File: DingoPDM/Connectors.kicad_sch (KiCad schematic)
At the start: 13 parts, among them J1 RedCubeTerminal, J2 RedCubeTerminal, J3 Conn_01x12, J5 USB_C_Receptacle_USB2.0

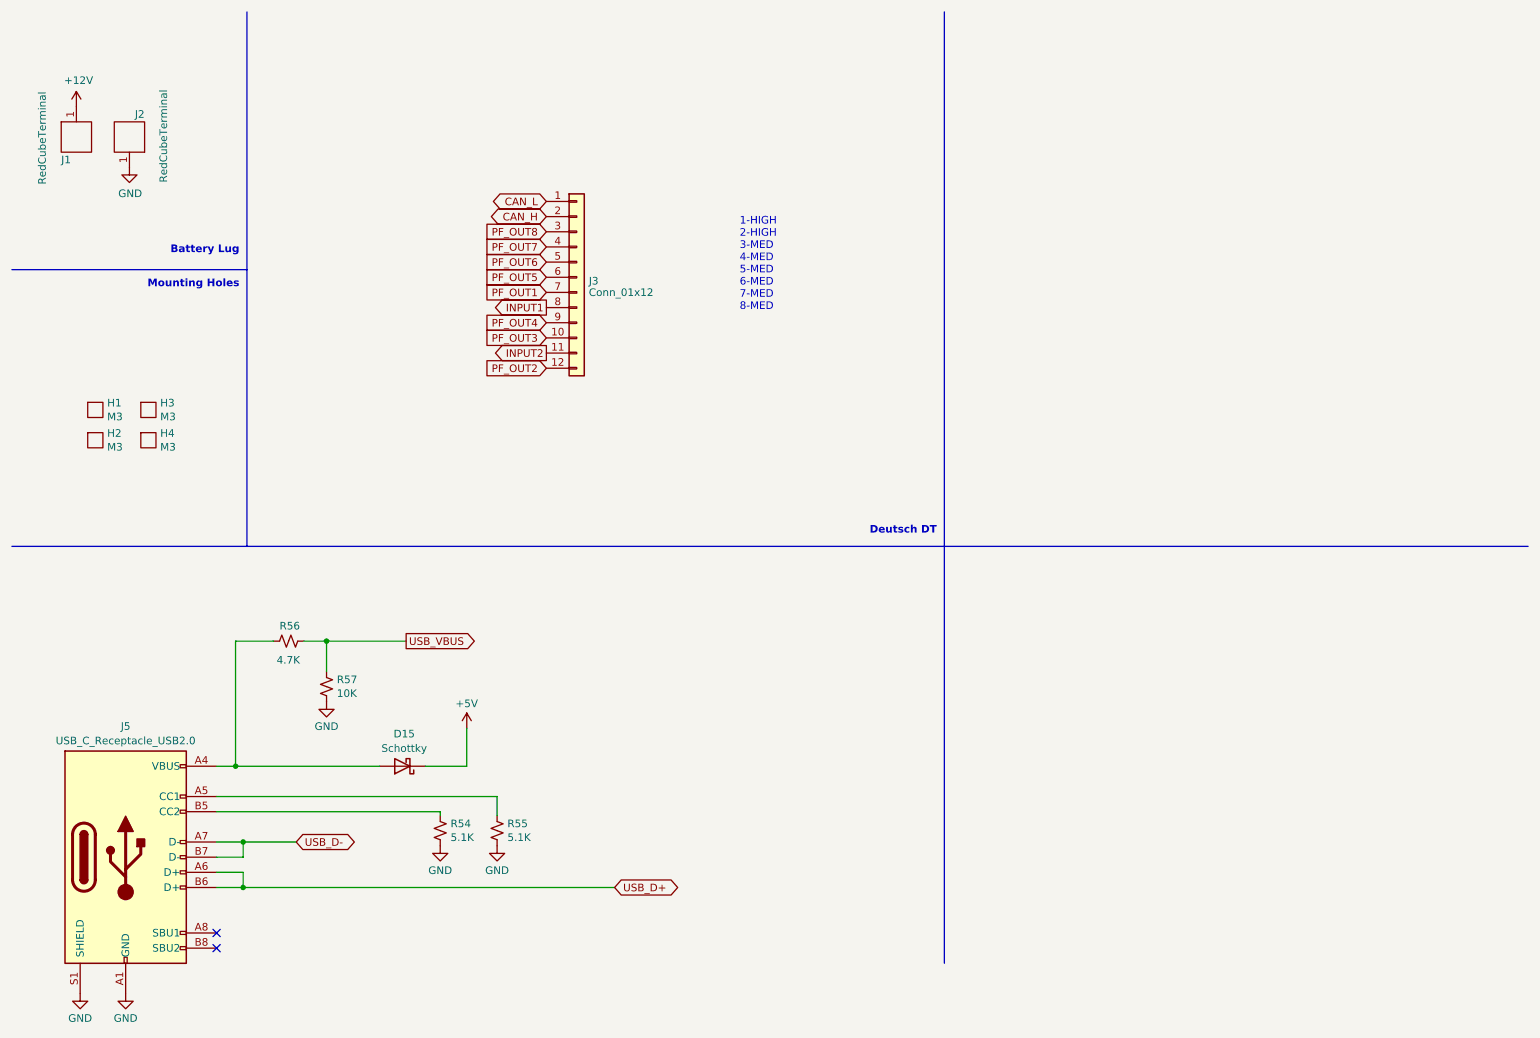
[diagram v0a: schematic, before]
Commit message: Modified PCB for 10ch PDM board
I modified the original dingoPDM for 10 channels. The board has been manufactured, tested and works but after mounting I decided that it doesn't suit my needs for the current build. I may develop it further in the future, make it pretty etc but for now I am marking this project as stale.
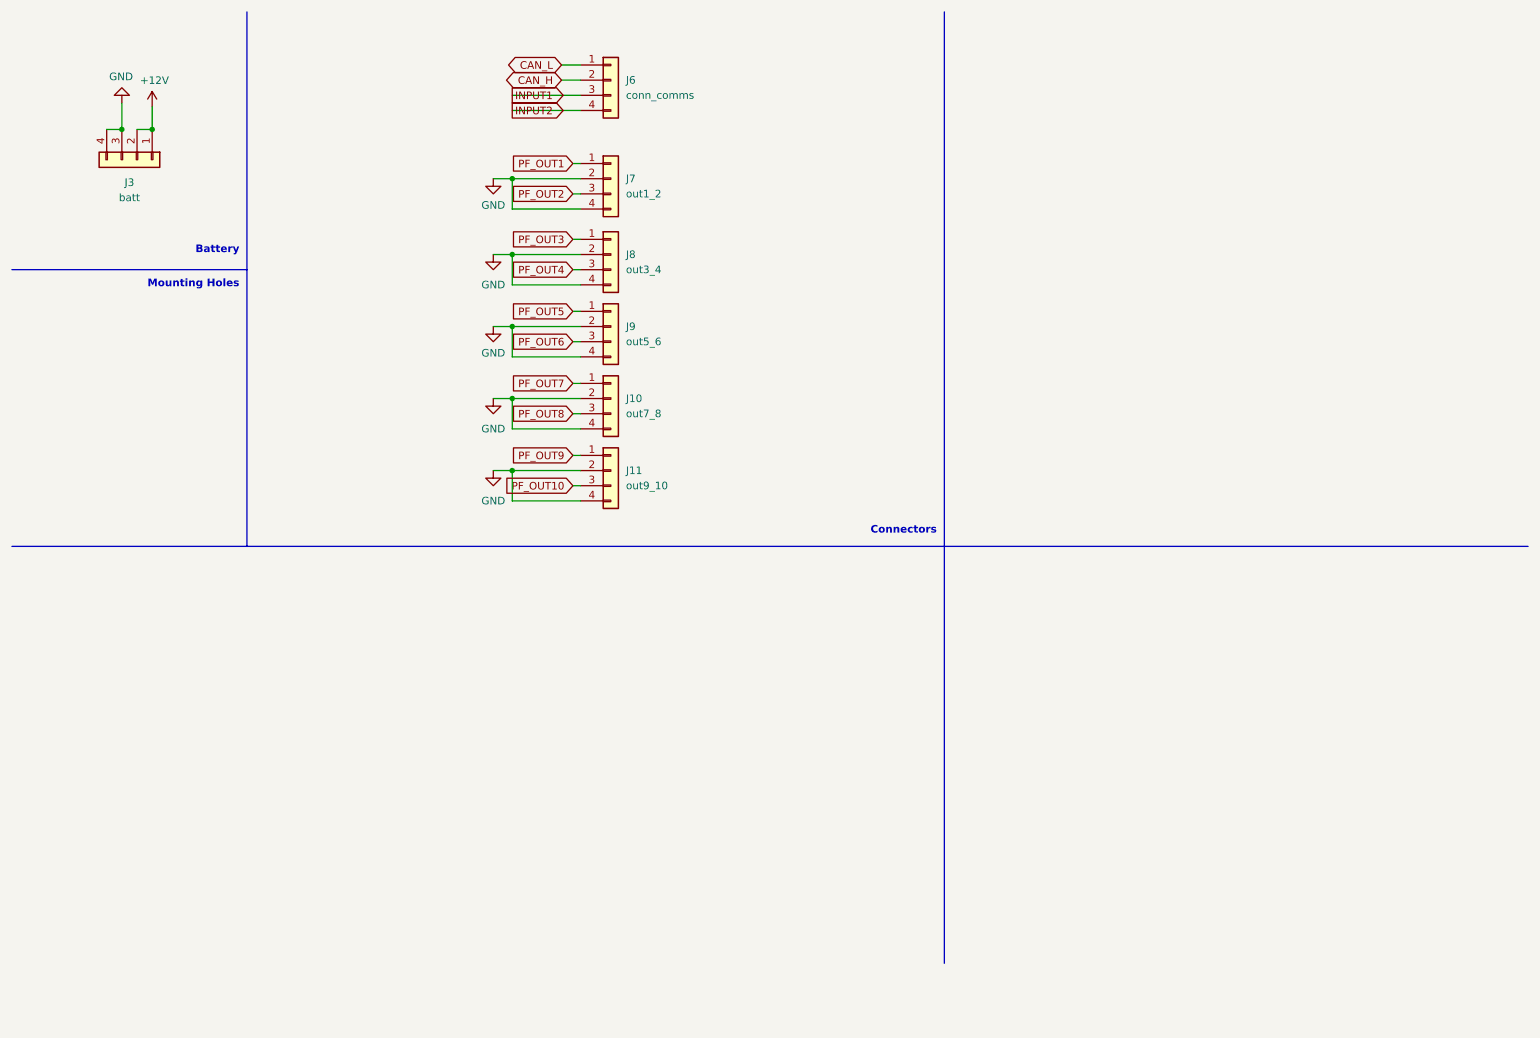
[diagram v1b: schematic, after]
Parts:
- removed D15: Schottky, Diode_SMD:D_SOD-123, symbol Device:D_Schottky
- removed H1, H2, H3, H4: M3, MountingHole:MountingHole_3.2mm_M3_ISO7380_Pad, symbol DingoPDM-rescue:M3-MountingHoles
- removed J1, J2: RedCubeTerminal, dingoPDM:M6_Hole_8Pin_7461084, symbol RedCube:RedCubeTerminal
- removed J3: Conn_01x12, dingoPDM:DT15-12PA, symbol Connector_Generic:Conn_01x12
- removed J5: USB_C_Receptacle_USB2.0, Connector_USB:USB_C_Receptacle_GCT_USB4085, symbol Connector:USB_C_Receptacle_USB2.0
- removed R54, R55: 5.1K, Resistor_SMD:R_0805_2012Metric, symbol Device:R_Small_US
- removed R56: 4.7K, Resistor_SMD:R_0805_2012Metric, symbol Device:R_Small_US
- removed R57: 10K, Resistor_SMD:R_0805_2012Metric, symbol Device:R_Small_US
- added J10: out7_8, DF_Conn:DIP-8_300_ELL, symbol Connector_Generic:Conn_01x04
- added J11: out9_10, DF_Conn:DIP-8_300_ELL, symbol Connector_Generic:Conn_01x04
- added J3: batt, DF_Conn:DIP-8_300_ELL, symbol Connector_Generic:Conn_01x04
- added J6: conn_comms, DF_Conn:DIP-8_300_ELL, symbol Connector_Generic:Conn_01x04
- added J7: out1_2, DF_Conn:DIP-8_300_ELL, symbol Connector_Generic:Conn_01x04
- added J8: out3_4, DF_Conn:DIP-8_300_ELL, symbol Connector_Generic:Conn_01x04
- added J9: out5_6, DF_Conn:DIP-8_300_ELL, symbol Connector_Generic:Conn_01x04
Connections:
- net +12V: now also J3.1 (Pin_1), J3.2 (Pin_2)
- net CAN_H: now also J6.2 (Pin_2)
- net CAN_L: now also J6.1 (Pin_1)
- net GND: now also J10.2 (Pin_2), J10.4 (Pin_4), J11.2 (Pin_2), J11.4 (Pin_4), J3.3 (Pin_3), J3.4 (Pin_4), J7.2 (Pin_2), J7.4 (Pin_4), J8.2 (Pin_2), J8.4 (Pin_4), J9.2 (Pin_2), J9.4 (Pin_4)
- net INPUT1: now also J6.3 (Pin_3)
- net INPUT2: now also J6.4 (Pin_4)
- net PF_OUT1: now also J7.1 (Pin_1)
- net PF_OUT2: now also J7.3 (Pin_3)
- net PF_OUT3: now also J8.1 (Pin_1)
- net PF_OUT4: now also J8.3 (Pin_3)
- net PF_OUT5: now also J9.1 (Pin_1)
- net PF_OUT6: now also J9.3 (Pin_3)
- net PF_OUT7: now also J10.1 (Pin_1)
- net PF_OUT8: now also J10.3 (Pin_3)
- new net PF_OUT10: J11.3 (Pin_3)
- new net PF_OUT9: J11.1 (Pin_1)
- no-connect marks 2 -> 0
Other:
- note added: "Battery"
- note added: "Connectors"
- note removed: "1-HIGH 2-HIGH 3-MED 4-MED 5-MED 6-MED 7-MED 8-MED"
- note removed: "Battery Lug"
- note removed: "Deutsch DT"
